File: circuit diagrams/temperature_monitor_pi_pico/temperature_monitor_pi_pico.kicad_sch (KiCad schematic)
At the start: 5 parts

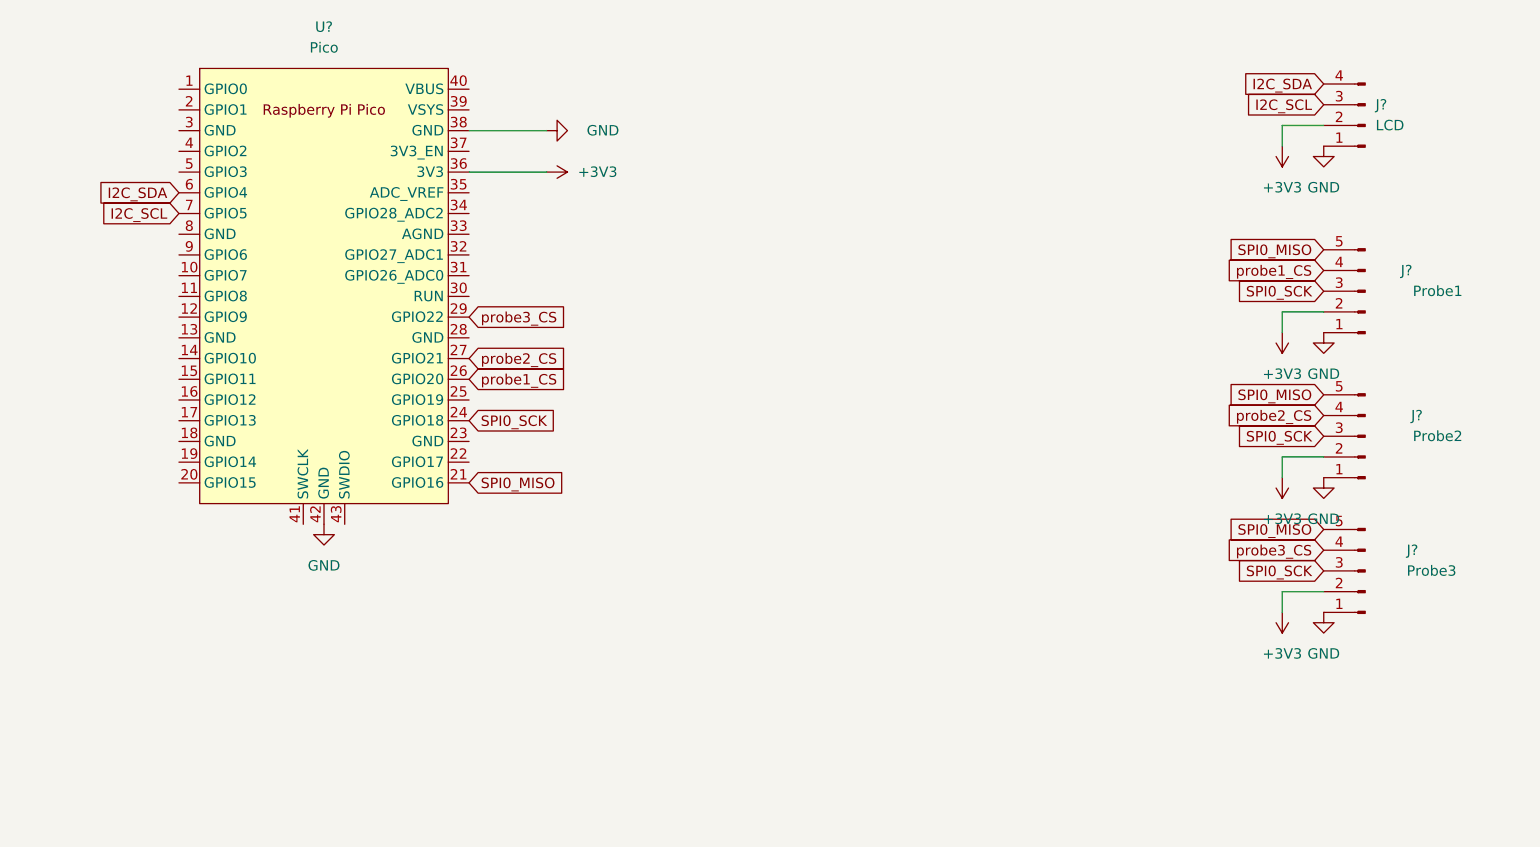
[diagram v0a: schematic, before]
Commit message: added thermal probe for reading air temperature
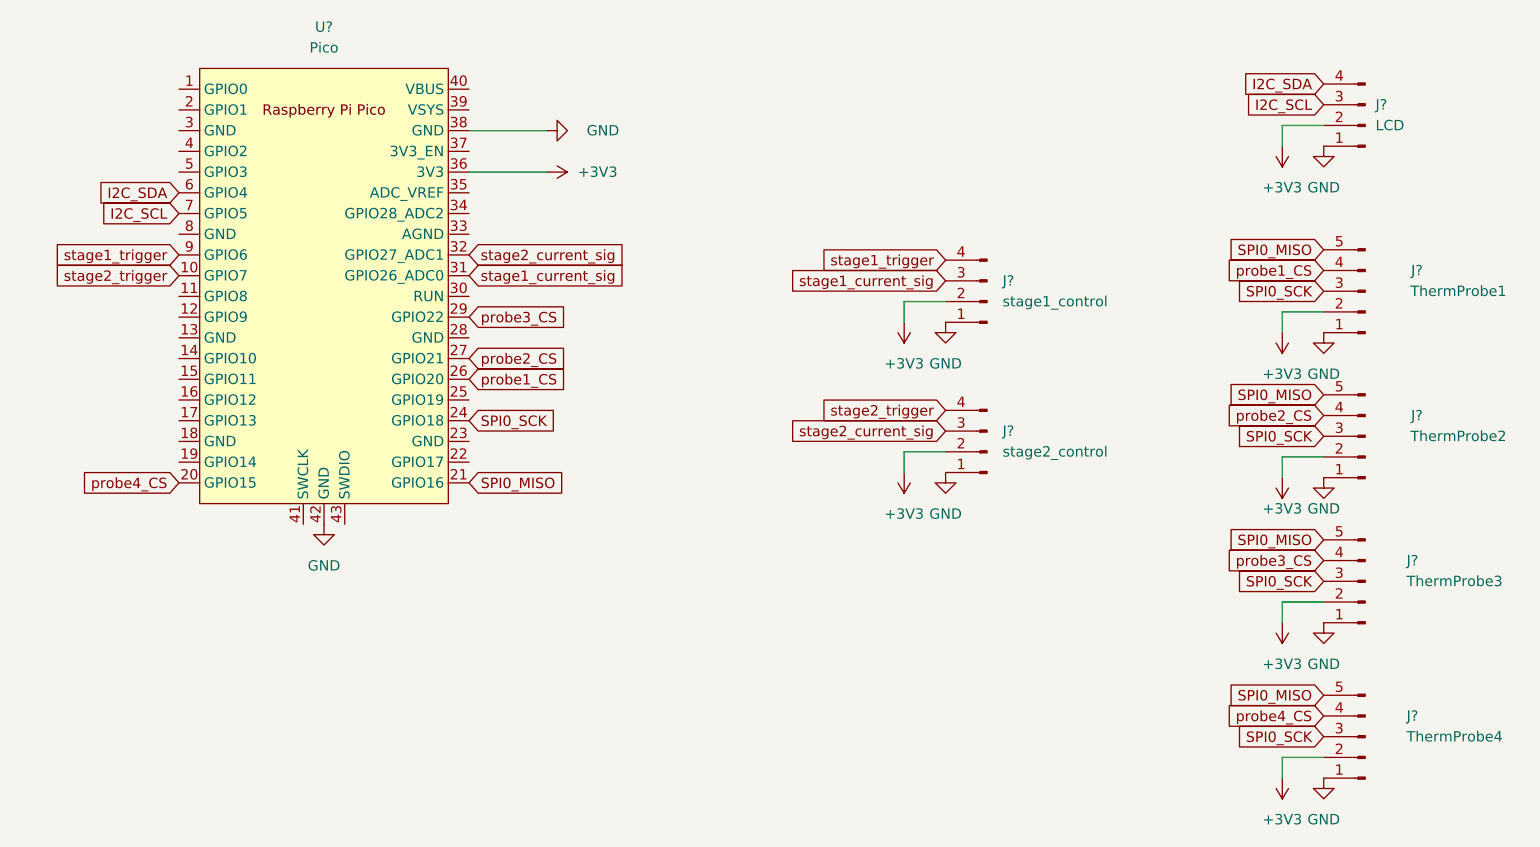
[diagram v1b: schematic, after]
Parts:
- added J?: ThermProbe4, symbol Connector:Conn_01x05_Male
- added J?: stage2_control, symbol Connector:Conn_01x04_Male
- added J?: stage1_control, symbol Connector:Conn_01x04_Male
- J?: value Probe1 -> ThermProbe1
- J?: value Probe3 -> ThermProbe3
- J?: value Probe2 -> ThermProbe2
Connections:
- net +3V3: now also J?.2 (Pin_2), J?.2 (Pin_2), J?.2 (Pin_2)
- net GND: now also J?.1 (Pin_1), J?.1 (Pin_1), J?.1 (Pin_1)
- net SPI0_MISO: now also J?.5 (Pin_5)
- net SPI0_SCK: now also J?.3 (Pin_3)
- net stage2_trigger: now reaches U?.10 (GPIO7)
- net stage2_trigger: now also J?.4 (Pin_4)
- net probe4_CS: now reaches U?.20 (GPIO15)
- net probe4_CS: now also J?.4 (Pin_4)
- net stage1_current_sig: now reaches U?.31 (GPIO26_ADC0)
- net stage1_current_sig: now also J?.3 (Pin_3)
- net stage2_current_sig: now reaches U?.32 (GPIO27_ADC1)
- net stage2_current_sig: now also J?.3 (Pin_3)
- net stage1_trigger: now reaches U?.9 (GPIO6)
- net stage1_trigger: now also J?.4 (Pin_4)
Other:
- moved on the sheet: J?
